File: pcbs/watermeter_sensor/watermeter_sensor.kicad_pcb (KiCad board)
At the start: 2 copper layers, 32.5 x 18 mm, 15 parts, among them J1 Conn_01x06, U1 LDC2112, U2 MCP1811A

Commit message: Add Zigbee Microcontroller design files
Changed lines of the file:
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@@
       (sketchpadsonfab false)
       (subtractmaskfromsilk true)
-      (outputformat 1)
+      (outputformat 4)
       (mirror false)
       (drillshape 0)
@@
     (fp_line (start 1 -0.625) (end 1 0.625) (layer "F.Fab") (width 0.1))
     (fp_line (start 1 0.625) (end -1 0.625) (layer "F.Fab") (width 0.1))
-    (pad "1" smd roundrect locked (at -0.9125 0) (size 1.025 1.4) (layers "F.Cu" "F.Paste" "F.Mask") (roundrect_rratio 0.243902)
+    (pad "1" smd roundrect locked (at -0.9125 0) (size 1.025 1.4) (layers "F.Cu" "F.Paste" "F.Mask") (roundrect_rratio 0.243902439)
       (net 1 "VCC"))
-    (pad "2" smd roundrect locked (at 0.9125 0) (size 1.025 1.4) (layers "F.Cu" "F.Paste" "F.Mask") (roundrect_rratio 0.243902)
+    (pad "2" smd roundrect locked (at 0.9125 0) (size 1.025 1.4) (layers "F.Cu" "F.Paste" "F.Mask") (roundrect_rratio 0.243902439)
       (net 9 "/SCL"))
     (model "${KICAD6_3DMODEL_DIR}/Resistor_SMD.3dshapes/R_0805_2012Metric.wrl"
@@
     (fp_line (start -1 -0.625) (end 1 -0.625) (layer "F.Fab") (width 0.1))
     (fp_line (start 1 -0.625) (end 1 0.625) (layer "F.Fab") (width 0.1))
-    (pad "1" smd roundrect locked (at -0.9125 0) (size 1.025 1.4) (layers "F.Cu" "F.Paste" "F.Mask") (roundrect_rratio 0.243902)
+    (pad "1" smd roundrect locked (at -0.9125 0) (size 1.025 1.4) (layers "F.Cu" "F.Paste" "F.Mask") (roundrect_rratio 0.243902439)
       (net 1 "VCC"))
-    (pad "2" smd roundrect locked (at 0.9125 0) (size 1.025 1.4) (layers "F.Cu" "F.Paste" "F.Mask") (roundrect_rratio 0.243902)
+    (pad "2" smd roundrect locked (at 0.9125 0) (size 1.025 1.4) (layers "F.Cu" "F.Paste" "F.Mask") (roundrect_rratio 0.243902439)
       (net 10 "/SDA"))
     (model "${KICAD6_3DMODEL_DIR}/Resistor_SMD.3dshapes/R_0805_2012Metric.wrl"

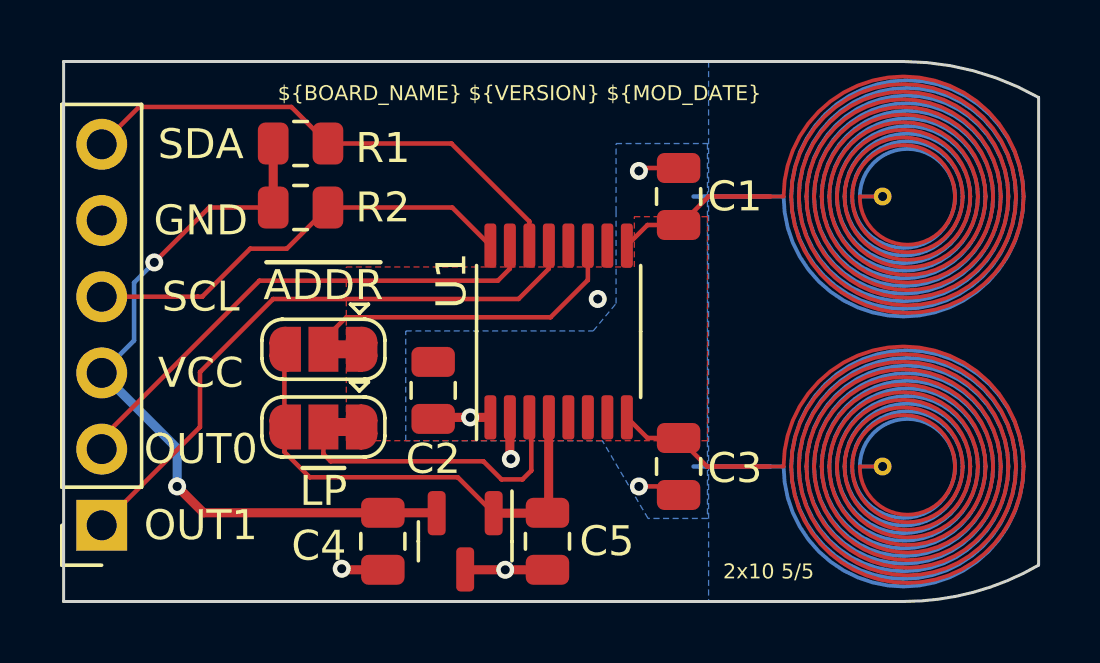
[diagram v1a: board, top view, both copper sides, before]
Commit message: Watermeter v1.1 (#6)
* Update Arduino library
* PCB Changes v1.1:
- changed LDO
- some footprints changed to 0603
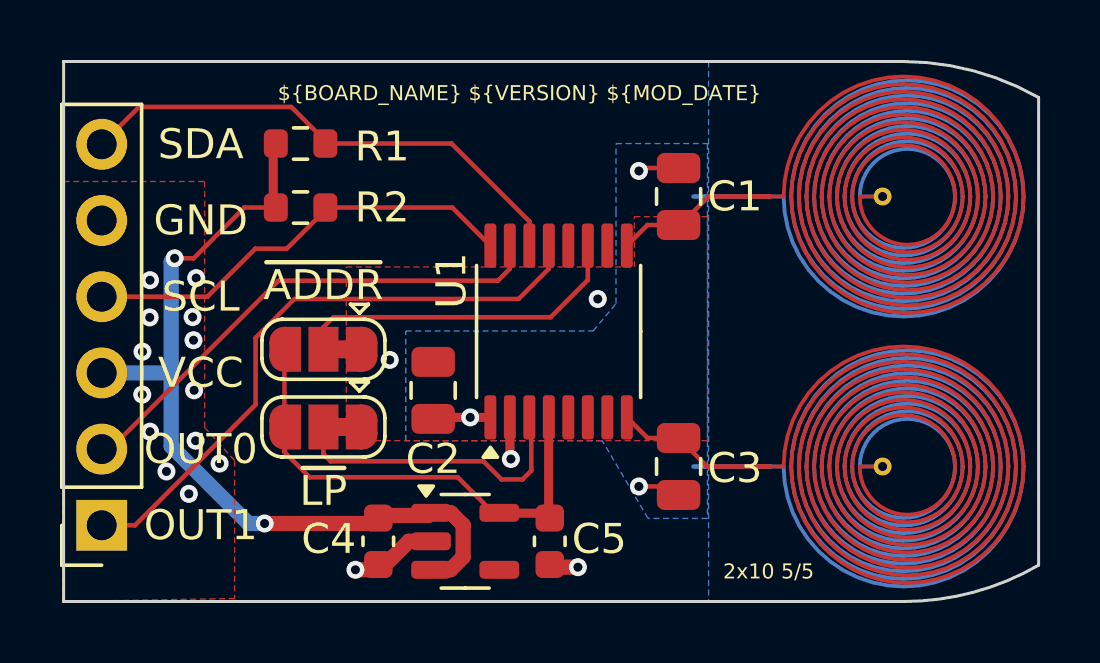
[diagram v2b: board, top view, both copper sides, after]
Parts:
- C4, C5: footprint Capacitor_SMD:C_0805_2012Metric -> Capacitor_SMD:C_0603_1608Metric
- R1, R2: footprint Resistor_SMD:R_0805_2012Metric -> Resistor_SMD:R_0603_1608Metric
- U2: value MCP1811A -> AP7354-18W5; footprint Package_TO_SOT_SMD:SOT-23 -> Package_TO_SOT_SMD:TSOT-23-5
- moved C4 0.15 mm to (110.5, 98.0)
- moved C5 0.08 mm to (116.2, 98.0)
- turned U2 to 0 degrees
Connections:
- U2 pad 1: +1V8 -> VCC
- U2 pad 2: VCC -> GND
- U2 pad 3: GND -> VCC
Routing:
- net VCC: track 25.1 -> 27.8 mm
- net GND: track 5.54 -> 5.33 mm, vias 4 -> 18
